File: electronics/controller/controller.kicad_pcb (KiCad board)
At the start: 2 copper layers, 12.7 x 12.7 mm, 2 parts

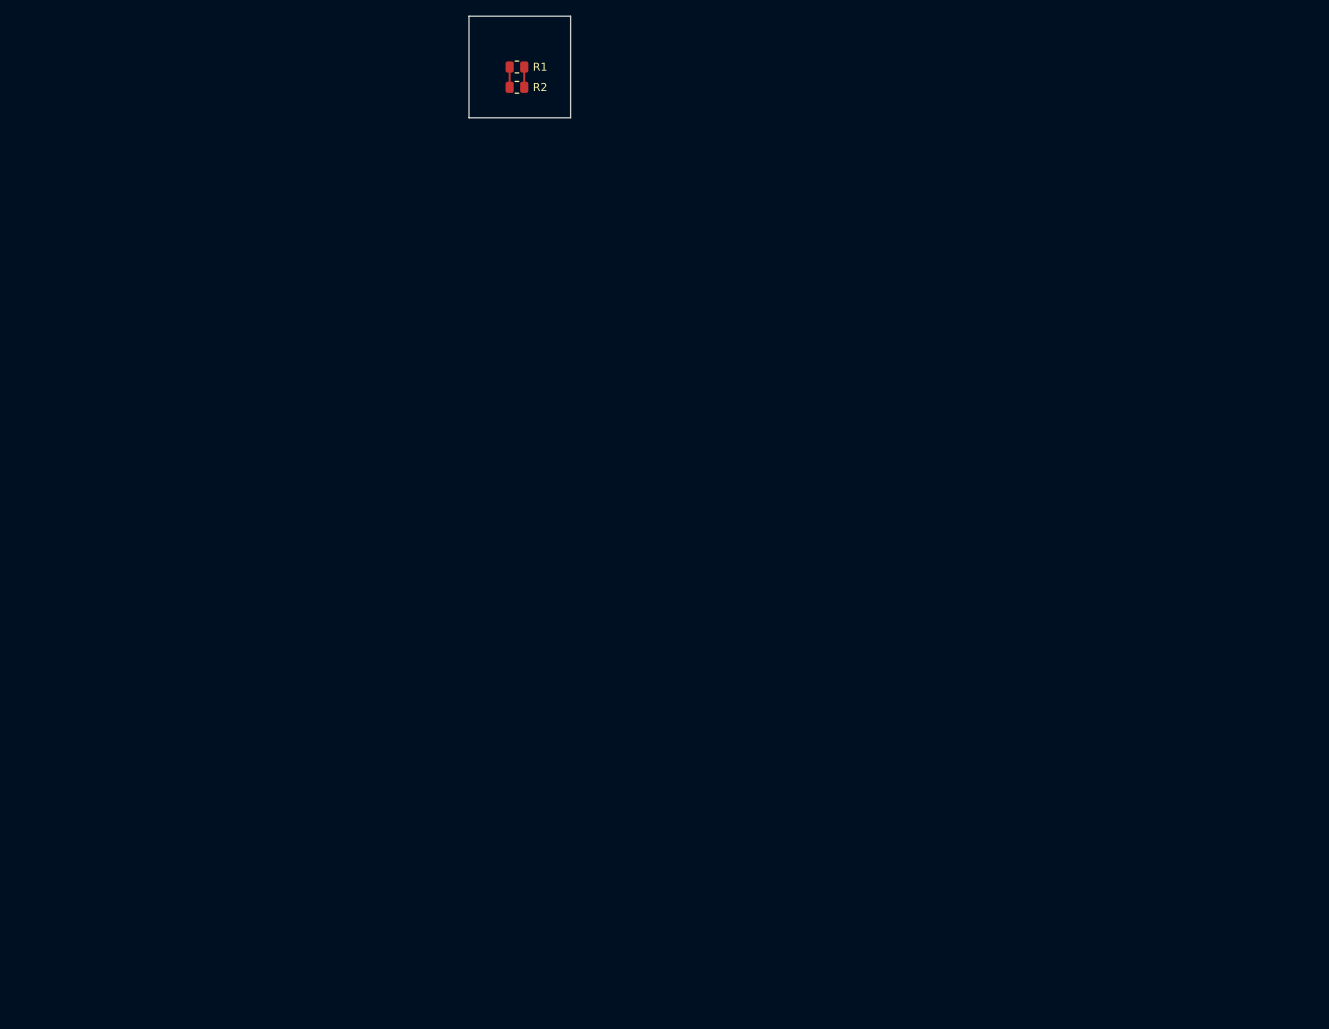
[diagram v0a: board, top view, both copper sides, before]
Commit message: Update PCB design to nearly finished design.
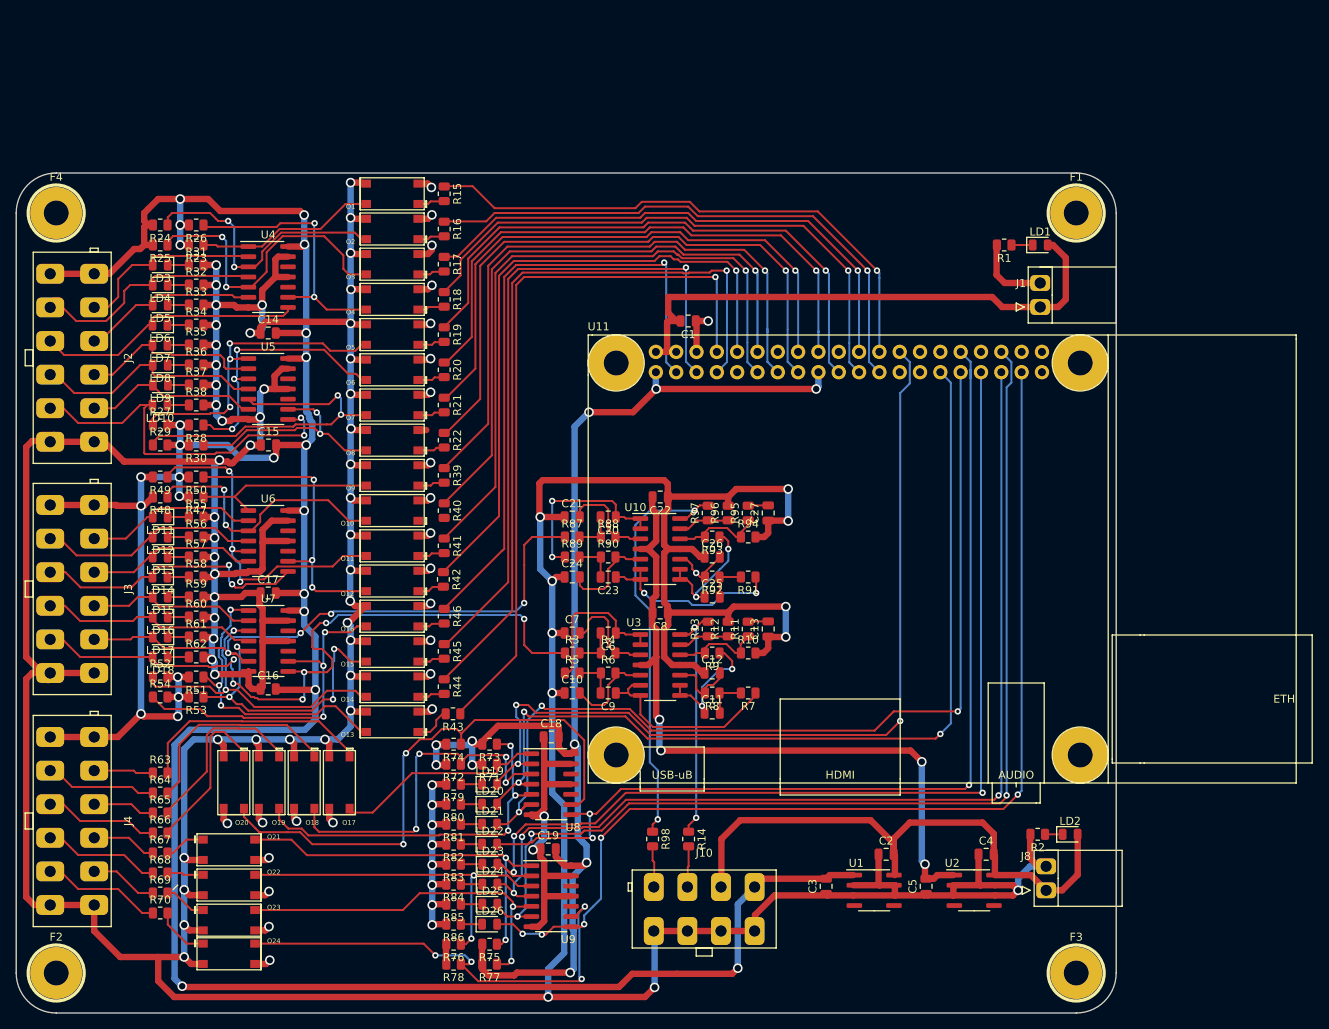
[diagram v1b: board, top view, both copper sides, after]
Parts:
- added C1: 100n, Capacitor_SMD:C_0805_2012Metric, F.Cu at (129.0, 63.5)
- added C10: 1u, Capacitor_SMD:C_0805_2012Metric, F.Cu at (114.5, 110.0)
- added C11: 1u, Capacitor_SMD:C_0805_2012Metric, F.Cu at (132.0, 112.5)
- added C12: 1u, Capacitor_SMD:C_0805_2012Metric, F.Cu at (132.0, 107.5)
- added C13: 1u, Capacitor_SMD:C_0805_2012Metric, F.Cu at (139.0, 102.0)
- added C14: 100n, Capacitor_SMD:C_0805_2012Metric, F.Cu at (76.5, 65.0)
- added C15: 100n, Capacitor_SMD:C_0805_2012Metric, F.Cu at (76.5, 79.0)
- added C16: 100n, Capacitor_SMD:C_0805_2012Metric, F.Cu at (76.5, 109.5)
- added C17: 100n, Capacitor_SMD:C_0805_2012Metric, F.Cu at (76.5, 97.5)
- added C18: 100n, Capacitor_SMD:C_0805_2012Metric, F.Cu at (111.9, 115.5)
- added C19: 100n, Capacitor_SMD:C_0805_2012Metric, F.Cu at (111.5, 129.5)
- added C2: 100n, Capacitor_SMD:C_0805_2012Metric, F.Cu at (153.7, 130.2)
- added C20: 1u, Capacitor_SMD:C_0805_2012Metric, F.Cu at (119.0, 88.0)
- added C21: 1u, Capacitor_SMD:C_0805_2012Metric, F.Cu at (114.5, 88.0)
- added C22: 100n, Capacitor_SMD:C_0805_2012Metric, F.Cu at (125.5, 85.5)
- added C23: 1u, Capacitor_SMD:C_0805_2012Metric, F.Cu at (119.0, 95.5)
- added C24: 1u, Capacitor_SMD:C_0805_2012Metric, F.Cu at (114.5, 95.5)
- added C25: 1u, Capacitor_SMD:C_0805_2012Metric, F.Cu at (132.0, 98.0)
- added C26: 1u, Capacitor_SMD:C_0805_2012Metric, F.Cu at (132.0, 93.0)
- added C27: 1u, Capacitor_SMD:C_0805_2012Metric, F.Cu at (139.0, 87.5)
- added C3: 100n, Capacitor_SMD:C_0805_2012Metric, F.Cu at (146.2, 134.2)
- added C4: 100n, Capacitor_SMD:C_0805_2012Metric, F.Cu at (166.2, 130.2)
- added C5: 100n, Capacitor_SMD:C_0805_2012Metric, F.Cu at (158.7, 134.2)
- added C6: 1u, Capacitor_SMD:C_0805_2012Metric, F.Cu at (119.0, 102.5)
- added C7: 1u, Capacitor_SMD:C_0805_2012Metric, F.Cu at (114.5, 102.5)
- added C8: 100n, Capacitor_SMD:C_0805_2012Metric, F.Cu at (125.5, 100.0)
- added C9: 1u, Capacitor_SMD:C_0805_2012Metric, F.Cu at (119.0, 110.0)
- added F1: M3, mechanical:M3, F.Cu at (177.5, 50.0)
- added F2: M3, mechanical:M3, F.Cu at (50.0, 145.0)
- added F3: M3, mechanical:M3, F.Cu at (177.5, 145.0)
- added F4: M3, mechanical:M3, F.Cu at (50.0, 50.0)
- added J1: SCREW2, wago_connectors:WAGO_MCS_MINI_02, F.Cu at (173.0, 60.2)
- added J10: TEVALULOK8W, te-connectivity_val-u-lok_vertical:te-connectivity_val-u-lok_vertical_8_1586768-8, F.Cu at (131.0, 137.0)
- added J2: TEVALULOK12W, te-connectivity_val-u-lok_vertical:te-connectivity_val-u-lok_vertical_12_1-1586768-2, F.Cu at (52.0, 68.1)
- added J3: TEVALULOK12W, te-connectivity_val-u-lok_vertical:te-connectivity_val-u-lok_vertical_12_1-1586768-2, F.Cu at (52.0, 97.0)
- added J4: TEVALULOK12W, te-connectivity_val-u-lok_vertical:te-connectivity_val-u-lok_vertical_12_1-1586768-2, F.Cu at (52.0, 126.0)
- added J8: SCREW2, wago_connectors:WAGO_MCS_MINI_02, F.Cu at (173.7, 133.2)
- added LD1: LED, LED_SMD:LED_0805_2012Metric, F.Cu at (173.0, 54.0)
- added LD10: LED, LED_SMD:LED_0805_2012Metric, F.Cu at (63.0, 74.0)
- added LD11: LED, LED_SMD:LED_0805_2012Metric, F.Cu at (63.0, 88.0)
- added LD12: LED, LED_SMD:LED_0805_2012Metric, F.Cu at (63.0, 90.5)
- added LD13: LED, LED_SMD:LED_0805_2012Metric, F.Cu at (63.0, 93.0)
- added LD14: LED, LED_SMD:LED_0805_2012Metric, F.Cu at (63.0, 95.5)
- added LD15: LED, LED_SMD:LED_0805_2012Metric, F.Cu at (63.0, 98.0)
- added LD16: LED, LED_SMD:LED_0805_2012Metric, F.Cu at (63.0, 100.5)
- added LD17: LED, LED_SMD:LED_0805_2012Metric, F.Cu at (63.0, 103.0)
- added LD18: LED, LED_SMD:LED_0805_2012Metric, F.Cu at (63.0, 105.5)
- added LD19: LED, LED_SMD:LED_0805_2012Metric, F.Cu at (104.2, 121.4)
- added LD2: LED, LED_SMD:LED_0805_2012Metric, F.Cu at (176.7, 127.7)
- added LD20: LED, LED_SMD:LED_0805_2012Metric, F.Cu at (104.2, 123.9)
- added LD21: LED, LED_SMD:LED_0805_2012Metric, F.Cu at (104.2, 126.4)
- added LD22: LED, LED_SMD:LED_0805_2012Metric, F.Cu at (104.2, 128.9)
- added LD23: LED, LED_SMD:LED_0805_2012Metric, F.Cu at (104.2, 131.4)
- added LD24: LED, LED_SMD:LED_0805_2012Metric, F.Cu at (104.2, 133.9)
- added LD25: LED, LED_SMD:LED_0805_2012Metric, F.Cu at (104.2, 136.4)
- added LD26: LED, LED_SMD:LED_0805_2012Metric, F.Cu at (104.2, 138.9)
- added LD3: LED, LED_SMD:LED_0805_2012Metric, F.Cu at (63.0, 56.5)
- added LD4: LED, LED_SMD:LED_0805_2012Metric, F.Cu at (63.0, 59.0)
- added LD5: LED, LED_SMD:LED_0805_2012Metric, F.Cu at (63.0, 61.5)
- added LD6: LED, LED_SMD:LED_0805_2012Metric, F.Cu at (63.0, 64.0)
- added LD7: LED, LED_SMD:LED_0805_2012Metric, F.Cu at (63.0, 66.5)
- added LD8: LED, LED_SMD:LED_0805_2012Metric, F.Cu at (63.0, 69.0)
- added LD9: LED, LED_SMD:LED_0805_2012Metric, F.Cu at (63.0, 71.5)
- added O1: VOM617A-4T, smd:VOMOPTO, F.Cu at (92.0, 47.6)
- added O10: VOM617A-4T, smd:VOMOPTO, F.Cu at (92.0, 87.2)
- added O11: VOM617A-4T, smd:VOMOPTO, F.Cu at (92.0, 91.6)
- added O12: VOM617A-4T, smd:VOMOPTO, F.Cu at (92.0, 96.0)
- added O13: VOM617A-4T, smd:VOMOPTO, F.Cu at (92.0, 113.6)
- added O14: VOM617A-4T, smd:VOMOPTO, F.Cu at (92.0, 109.2)
- added O15: VOM617A-4T, smd:VOMOPTO, F.Cu at (92.0, 104.8)
- added O16: VOM617A-4T, smd:VOMOPTO, F.Cu at (92.0, 100.4)
- added O17: VOM617A-4T, smd:VOMOPTO, F.Cu at (85.4, 121.2)
- added O18: VOM617A-4T, smd:VOMOPTO, F.Cu at (81.0, 121.2)
- added O19: VOM617A-4T, smd:VOMOPTO, F.Cu at (76.6, 121.2)
- added O2: VOM617A-4T, smd:VOMOPTO, F.Cu at (92.0, 52.0)
- added O20: VOM617A-4T, smd:VOMOPTO, F.Cu at (72.2, 121.2)
- added O21: VOM617A-4T, smd:VOMOPTO, F.Cu at (71.6, 129.6)
- added O22: VOM617A-4T, smd:VOMOPTO, F.Cu at (71.6, 134.0)
- added O23: VOM617A-4T, smd:VOMOPTO, F.Cu at (71.6, 138.4)
- added O24: VOM617A-4T, smd:VOMOPTO, F.Cu at (71.6, 142.6)
- added O3: VOM617A-4T, smd:VOMOPTO, F.Cu at (92.0, 56.4)
- added O4: VOM617A-4T, smd:VOMOPTO, F.Cu at (92.0, 60.8)
- added O5: VOM617A-4T, smd:VOMOPTO, F.Cu at (92.0, 65.2)
- added O6: VOM617A-4T, smd:VOMOPTO, F.Cu at (92.0, 69.6)
- added O7: VOM617A-4T, smd:VOMOPTO, F.Cu at (92.0, 74.0)
- added O8: VOM617A-4T, smd:VOMOPTO, F.Cu at (92.0, 78.4)
- added O9: VOM617A-4T, smd:VOMOPTO, F.Cu at (92.0, 82.8)
- added R10: 1k5, Resistor_SMD:R_0805_2012Metric, F.Cu at (136.5, 105.0)
- added R11: 120k, Resistor_SMD:R_0805_2012Metric, F.Cu at (136.5, 102.0)
- added R12: 1k5, Resistor_SMD:R_0805_2012Metric, F.Cu at (134.0, 102.0)
- added R13: 120k, Resistor_SMD:R_0805_2012Metric, F.Cu at (131.5, 102.0)
- added R14: 330R, Resistor_SMD:R_0805_2012Metric, F.Cu at (129.1, 128.2)
- added R15: 680R, Resistor_SMD:R_0805_2012Metric, F.Cu at (98.5, 47.6)
- added R16: 680R, Resistor_SMD:R_0805_2012Metric, F.Cu at (98.5, 52.0)
- added R17: 680R, Resistor_SMD:R_0805_2012Metric, F.Cu at (98.5, 56.4)
- added R18: 680R, Resistor_SMD:R_0805_2012Metric, F.Cu at (98.5, 60.8)
- added R19: 680R, Resistor_SMD:R_0805_2012Metric, F.Cu at (98.5, 65.2)
- added R20: 680R, Resistor_SMD:R_0805_2012Metric, F.Cu at (98.5, 69.6)
- added R21: 680R, Resistor_SMD:R_0805_2012Metric, F.Cu at (98.5, 74.0)
- added R22: 680R, Resistor_SMD:R_0805_2012Metric, F.Cu at (98.5, 78.4)
- added R23: 1k, Resistor_SMD:R_0805_2012Metric, F.Cu at (67.5, 54.0)
- added R24: 1k, Resistor_SMD:R_0805_2012Metric, F.Cu at (63.0, 51.5)
- added R25: 1k, Resistor_SMD:R_0805_2012Metric, F.Cu at (63.0, 54.0)
- added R26: 1k, Resistor_SMD:R_0805_2012Metric, F.Cu at (67.5, 51.5)
- added R27: 1k, Resistor_SMD:R_0805_2012Metric, F.Cu at (63.0, 76.5)
- added R28: 1k, Resistor_SMD:R_0805_2012Metric, F.Cu at (67.5, 76.5)
- added R29: 1k, Resistor_SMD:R_0805_2012Metric, F.Cu at (63.0, 79.0)
- added R3: 68k, Resistor_SMD:R_0805_2012Metric, F.Cu at (114.5, 105.0)
- added R30: 1k, Resistor_SMD:R_0805_2012Metric, F.Cu at (67.5, 79.0)
- added R31: RESISTOR, Resistor_SMD:R_0805_2012Metric, F.Cu at (67.5, 56.5)
- added R32: RESISTOR, Resistor_SMD:R_0805_2012Metric, F.Cu at (67.5, 59.0)
- added R33: RESISTOR, Resistor_SMD:R_0805_2012Metric, F.Cu at (67.5, 61.5)
- added R34: RESISTOR, Resistor_SMD:R_0805_2012Metric, F.Cu at (67.5, 64.0)
- added R35: RESISTOR, Resistor_SMD:R_0805_2012Metric, F.Cu at (67.5, 66.5)
- added R36: RESISTOR, Resistor_SMD:R_0805_2012Metric, F.Cu at (67.5, 69.0)
- added R37: RESISTOR, Resistor_SMD:R_0805_2012Metric, F.Cu at (67.5, 71.5)
- added R38: RESISTOR, Resistor_SMD:R_0805_2012Metric, F.Cu at (67.5, 74.0)
- added R39: 680R, Resistor_SMD:R_0805_2012Metric, F.Cu at (98.5, 82.8)
- added R4: 68k, Resistor_SMD:R_0805_2012Metric, F.Cu at (119.0, 105.0)
- added R40: 680R, Resistor_SMD:R_0805_2012Metric, F.Cu at (98.5, 87.2)
- added R41: 680R, Resistor_SMD:R_0805_2012Metric, F.Cu at (98.5, 91.6)
- added R42: 680R, Resistor_SMD:R_0805_2012Metric, F.Cu at (98.4, 95.8)
- added R43: 680R, Resistor_SMD:R_0805_2012Metric, F.Cu at (99.6, 112.6)
- added R44: 680R, Resistor_SMD:R_0805_2012Metric, F.Cu at (98.5, 109.2)
- added R45: 680R, Resistor_SMD:R_0805_2012Metric, F.Cu at (98.5, 104.8)
- added R46: 680R, Resistor_SMD:R_0805_2012Metric, F.Cu at (98.5, 100.4)
- added R47: 1k, Resistor_SMD:R_0805_2012Metric, F.Cu at (67.5, 85.5)
- added R48: 1k, Resistor_SMD:R_0805_2012Metric, F.Cu at (63.0, 85.5)
- added R49: 1k, Resistor_SMD:R_0805_2012Metric, F.Cu at (63.0, 83.0)
- added R5: 68k, Resistor_SMD:R_0805_2012Metric, F.Cu at (114.5, 107.5)
- added R50: 1k, Resistor_SMD:R_0805_2012Metric, F.Cu at (67.5, 83.0)
- added R51: 1k, Resistor_SMD:R_0805_2012Metric, F.Cu at (67.5, 108.0)
- added R52: 1k, Resistor_SMD:R_0805_2012Metric, F.Cu at (63.0, 108.0)
- added R53: 1k, Resistor_SMD:R_0805_2012Metric, F.Cu at (67.5, 110.5)
- added R54: 1k, Resistor_SMD:R_0805_2012Metric, F.Cu at (63.0, 110.5)
- added R55: RESISTOR, Resistor_SMD:R_0805_2012Metric, F.Cu at (67.5, 88.0)
- added R56: RESISTOR, Resistor_SMD:R_0805_2012Metric, F.Cu at (67.5, 90.5)
- added R57: RESISTOR, Resistor_SMD:R_0805_2012Metric, F.Cu at (67.5, 93.0)
- added R58: RESISTOR, Resistor_SMD:R_0805_2012Metric, F.Cu at (67.5, 95.5)
- added R59: RESISTOR, Resistor_SMD:R_0805_2012Metric, F.Cu at (67.5, 98.0)
- added R6: 68k, Resistor_SMD:R_0805_2012Metric, F.Cu at (119.0, 107.5)
- added R60: RESISTOR, Resistor_SMD:R_0805_2012Metric, F.Cu at (67.5, 100.5)
- added R61: RESISTOR, Resistor_SMD:R_0805_2012Metric, F.Cu at (67.5, 103.0)
- added R62: RESISTOR, Resistor_SMD:R_0805_2012Metric, F.Cu at (67.5, 105.5)
- added R63: 680R, Resistor_SMD:R_0805_2012Metric, F.Cu at (63.0, 120.0)
- added R64: 680R, Resistor_SMD:R_0805_2012Metric, F.Cu at (63.0, 122.5)
- added R65: 680R, Resistor_SMD:R_0805_2012Metric, F.Cu at (63.0, 125.0)
- added R66: 680R, Resistor_SMD:R_0805_2012Metric, F.Cu at (63.0, 127.5)
- added R67: 680R, Resistor_SMD:R_0805_2012Metric, F.Cu at (63.0, 130.0)
- added R68: 680R, Resistor_SMD:R_0805_2012Metric, F.Cu at (63.0, 132.5)
- added R69: 680R, Resistor_SMD:R_0805_2012Metric, F.Cu at (63.0, 135.0)
- added R7: 68k, Resistor_SMD:R_0805_2012Metric, F.Cu at (136.5, 110.0)
- added R70: 680R, Resistor_SMD:R_0805_2012Metric, F.Cu at (63.0, 137.5)
- added R71: 1k, Resistor_SMD:R_0805_2012Metric, F.Cu at (104.2, 118.9)
- added R72: 1k, Resistor_SMD:R_0805_2012Metric, F.Cu at (99.7, 118.9)
- added R73: 1k, Resistor_SMD:R_0805_2012Metric, F.Cu at (104.2, 116.4)
- added R74: 1k, Resistor_SMD:R_0805_2012Metric, F.Cu at (99.7, 116.4)
- added R75: 1k, Resistor_SMD:R_0805_2012Metric, F.Cu at (104.2, 141.4)
- added R76: 1k, Resistor_SMD:R_0805_2012Metric, F.Cu at (99.7, 141.4)
- added R77: 1k, Resistor_SMD:R_0805_2012Metric, F.Cu at (104.2, 143.9)
- added R78: 1k, Resistor_SMD:R_0805_2012Metric, F.Cu at (99.7, 143.9)
- added R79: RESISTOR, Resistor_SMD:R_0805_2012Metric, F.Cu at (99.7, 121.4)
- added R8: 68k, Resistor_SMD:R_0805_2012Metric, F.Cu at (132.0, 110.0)
- added R80: RESISTOR, Resistor_SMD:R_0805_2012Metric, F.Cu at (99.7, 123.9)
- added R81: RESISTOR, Resistor_SMD:R_0805_2012Metric, F.Cu at (99.7, 126.4)
- added R82: RESISTOR, Resistor_SMD:R_0805_2012Metric, F.Cu at (99.7, 128.9)
- added R83: RESISTOR, Resistor_SMD:R_0805_2012Metric, F.Cu at (99.7, 131.4)
- added R84: RESISTOR, Resistor_SMD:R_0805_2012Metric, F.Cu at (99.7, 133.9)
- added R85: RESISTOR, Resistor_SMD:R_0805_2012Metric, F.Cu at (99.7, 136.4)
- added R86: RESISTOR, Resistor_SMD:R_0805_2012Metric, F.Cu at (99.7, 138.9)
- added R87: 68k, Resistor_SMD:R_0805_2012Metric, F.Cu at (114.5, 90.5)
- added R88: 68k, Resistor_SMD:R_0805_2012Metric, F.Cu at (119.0, 90.5)
- added R89: 68k, Resistor_SMD:R_0805_2012Metric, F.Cu at (114.5, 93.0)
- added R9: 68k, Resistor_SMD:R_0805_2012Metric, F.Cu at (132.0, 105.0)
- added R90: 68k, Resistor_SMD:R_0805_2012Metric, F.Cu at (119.0, 93.0)
- added R91: 68k, Resistor_SMD:R_0805_2012Metric, F.Cu at (136.5, 95.5)
- added R92: 68k, Resistor_SMD:R_0805_2012Metric, F.Cu at (132.0, 95.5)
- added R93: 68k, Resistor_SMD:R_0805_2012Metric, F.Cu at (132.0, 90.5)
- added R94: 1k5, Resistor_SMD:R_0805_2012Metric, F.Cu at (136.5, 90.5)
- added R95: 120k, Resistor_SMD:R_0805_2012Metric, F.Cu at (136.5, 87.5)
- added R96: 1k5, Resistor_SMD:R_0805_2012Metric, F.Cu at (134.0, 87.5)
- added R97: 120k, Resistor_SMD:R_0805_2012Metric, F.Cu at (131.5, 87.5)
- added R98: 330R, Resistor_SMD:R_0805_2012Metric, F.Cu at (124.5, 128.2)
- added U1: 78L05SMD, Package_SO:SOIC-8_3.9x4.9mm_P1.27mm, F.Cu at (152.2, 134.7)
- added U10: MC33204, Package_SO:SOIC-14_3.9x8.7mm_P1.27mm, F.Cu at (125.5, 92.0)
- added U11: RPI40PIN, rpi_footprints:rpi-40pin, F.Cu at (127.5, 76.2)
- added U2: 78L10SMD, Package_SO:SOIC-8_3.9x4.9mm_P1.27mm, F.Cu at (164.7, 134.7)
- added U3: MC33204, Package_SO:SOIC-14_3.9x8.7mm_P1.27mm, F.Cu at (125.5, 106.5)
- added U4: 74HC14, Package_SO:SOIC-14_3.9x8.7mm_P1.27mm, F.Cu at (76.5, 58.0)
- added U5: 74HC14, Package_SO:SOIC-14_3.9x8.7mm_P1.27mm, F.Cu at (76.5, 72.0)
- added U6: 74HC14, Package_SO:SOIC-14_3.9x8.7mm_P1.27mm, F.Cu at (76.5, 91.0)
- added U7: 74HC14, Package_SO:SOIC-14_3.9x8.7mm_P1.27mm, F.Cu at (76.5, 103.5)
- added U8: 74HC14, Package_SO:SOIC-14_3.9x8.7mm_P1.27mm, F.Cu at (111.9, 121.4)
- added U9: 74HC14, Package_SO:SOIC-14_3.9x8.7mm_P1.27mm, F.Cu at (111.9, 135.4)
- R1: value 1k5 -> RESISTOR
- R2: value 470R -> 2k2
- moved R2 113.8 mm to (172.7, 127.7), turned to 180 degrees
- moved R1 64.8 mm to (168.5, 54.0), turned to 180 degrees
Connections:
- R1 pad 1: Net-(R1-Pad1) -> Net-(LD1-Pad1)
- R1 pad 2: Net-(R1-Pad2) -> GND
- R2 pad 1: Net-(R1-Pad1) -> Net-(LD2-Pad1)
- R2 pad 2: Net-(R1-Pad2) -> VSS
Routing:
- net VSS: track 0.00 -> 794.8 mm, vias 0 -> 60
- net VDD: track 0.00 -> 389.9 mm, vias 0 -> 25
- net /rpiconnectivity/3V3: track 0.00 -> 161.8 mm, vias 0 -> 10
- net /RPIIN7: track 0.00 -> 133.8 mm, vias 0 -> 3
- net /RPIIN8: track 0.00 -> 131.0 mm, vias 0 -> 5
- net /RPIIN6: track 0.00 -> 127.2 mm, vias 0 -> 3
- net /RPIIN5: track 0.00 -> 124.8 mm, vias 0 -> 3
- net /RPIIN4: track 0.00 -> 122.9 mm, vias 0 -> 3
- net GND: track 0.00 -> 120.5 mm, vias 0 -> 34
- net /RPIIN3: track 0.00 -> 118.5 mm, vias 0 -> 3
- net /RPIIN2: track 0.00 -> 116.3 mm, vias 0 -> 3
- net /RPIIN1: track 0.00 -> 110.6 mm, vias 0 -> 3
- net /RPIOUT14: track 0.00 -> 93.8 mm, vias 0 -> 1
- net /OUT16: track 0.00 -> 93.3 mm, vias 0 -> 6
- net /RPIOUT13: track 0.00 -> 91.8 mm, vias 0 -> 1
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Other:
- board size 12.7 x 12.7 mm -> 137.5 x 105 mm
- net class Default removed

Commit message: PCB zones added and fully routed
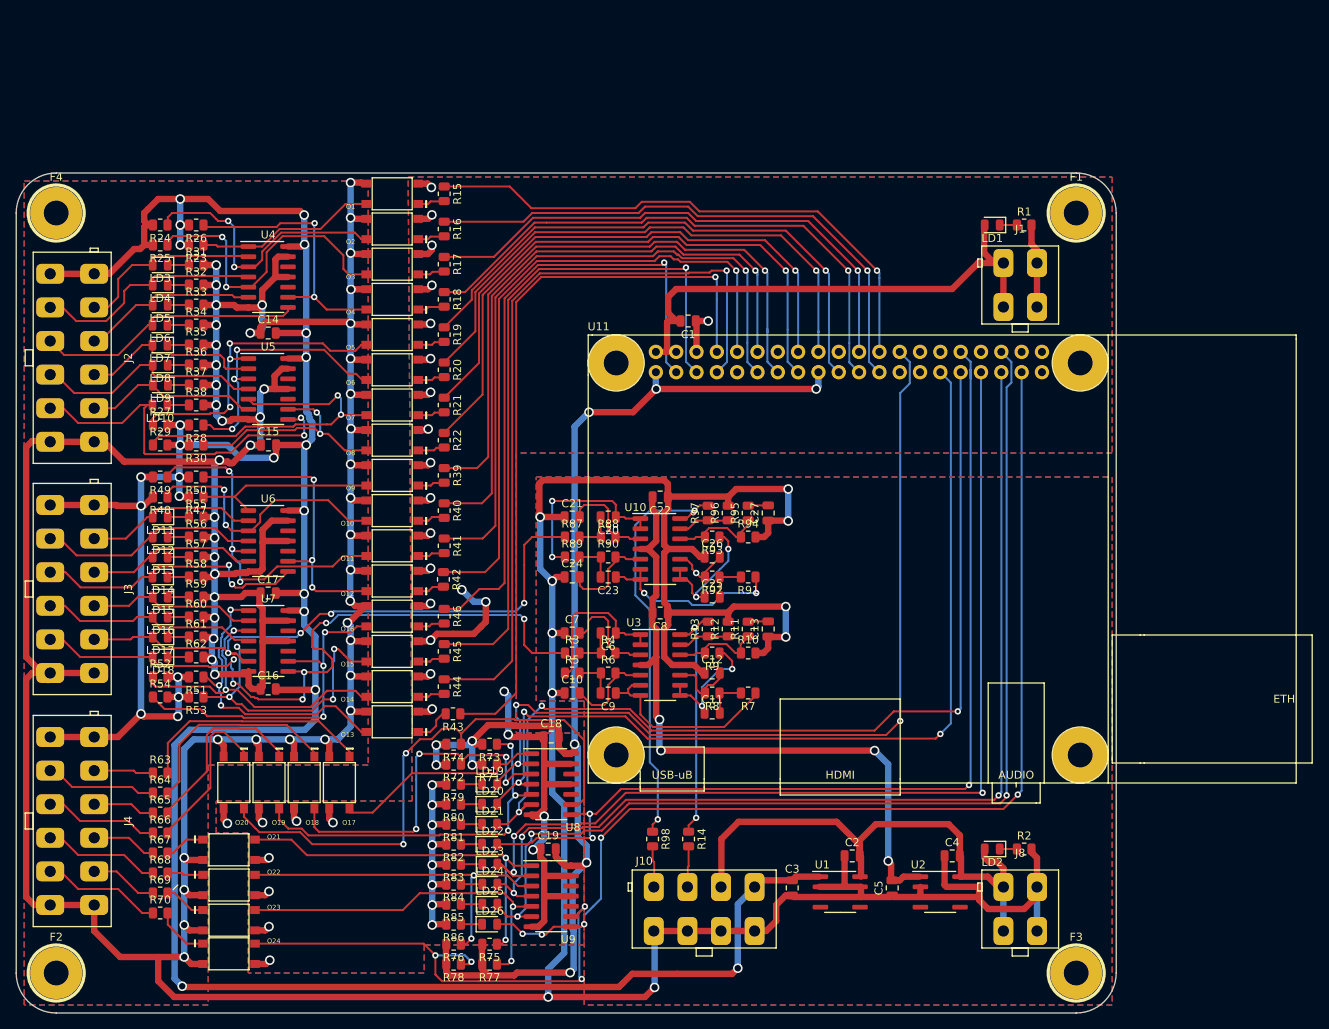
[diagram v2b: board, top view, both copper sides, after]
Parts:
- J1, J8: value SCREW2 -> TEVALULOK4W; footprint wago_connectors:WAGO_MCS_MINI_02 -> te-connectivity_val-u-lok_vertical:te-connectivity_val-u-lok_vertical_4_1586768-4
- moved LD2 9.91 mm to (167.0, 129.5), turned to 180 degrees
- moved LD1 6.50 mm to (167.0, 51.5), turned to 180 degrees
- moved J8 5.02 mm to (170.5, 137.0), turned to 0 degrees
- moved C2 4.25 mm to (149.5, 130.4)
- moved C3 4.25 mm to (142.0, 134.4)
- moved C4 4.25 mm to (162.0, 130.4)
- moved C5 4.25 mm to (154.5, 134.4)
- moved U1 4.25 mm to (148.0, 134.9)
- moved U2 4.25 mm to (160.5, 134.9)
- moved R1 3.54 mm to (171.0, 51.5), turned to 0 degrees
- moved J1 2.80 mm to (170.5, 59.0), turned to 0 degrees
- moved R2 2.50 mm to (171.0, 129.5), turned to 0 degrees
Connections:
- J1 pad 2: GND -> VCC
- J8 pad 2: VSS -> +12V
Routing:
- net GND: track 120.5 -> 145.8 mm, vias 34 -> 39
- net /rpiconnectivity/3V3: track 161.8 -> 169.2 mm
- net Net-(O24-Pad4): track 56.8 -> 61.9 mm
- net VDD: track 389.9 -> 385.6 mm
- net +10V: track 88.4 -> 84.2 mm
- net +12V: track 71.8 -> 68.3 mm
- net Net-(O10-Pad1): track 0.00 -> 3.49 mm
- net VCC: track 70.7 -> 67.6 mm
- net /RPIOUT12: track 81.5 -> 84.3 mm
- net /RPIOUT5: track 72.4 -> 69.8 mm
- net /RPIOUT6: track 71.7 -> 69.3 mm
- net /RPIOUT14: track 93.8 -> 96.1 mm
- net /RPIOUT7: track 72.4 -> 70.1 mm
- net /RPIOUT8: track 77.7 -> 75.5 mm
- net /RPIOUT15: track 85.5 -> 87.4 mm
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- added copper zone on B.Cu, net (none)
- added copper zone on F.Cu, net (none)
- added copper zone on B.Cu, net GND
- added copper zone on F.Cu, net GND
- added copper zone on B.Cu, net VSS
- added copper zone on F.Cu, net VSS

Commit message: Add JLCPCB fabrication output post order
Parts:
- R31, R32, R33, R34, R35, R36, R37, R38, R55, R56, R57, R58, R59, R60, R61, R62, R79, R80, R81, R82, R83, R84, R85, R86: value RESISTOR -> 330R
